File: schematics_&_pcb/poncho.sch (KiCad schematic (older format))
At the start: 4 parts, among them P1 CONN_20X2, P2 CONN_20X2, P3 ESP8266

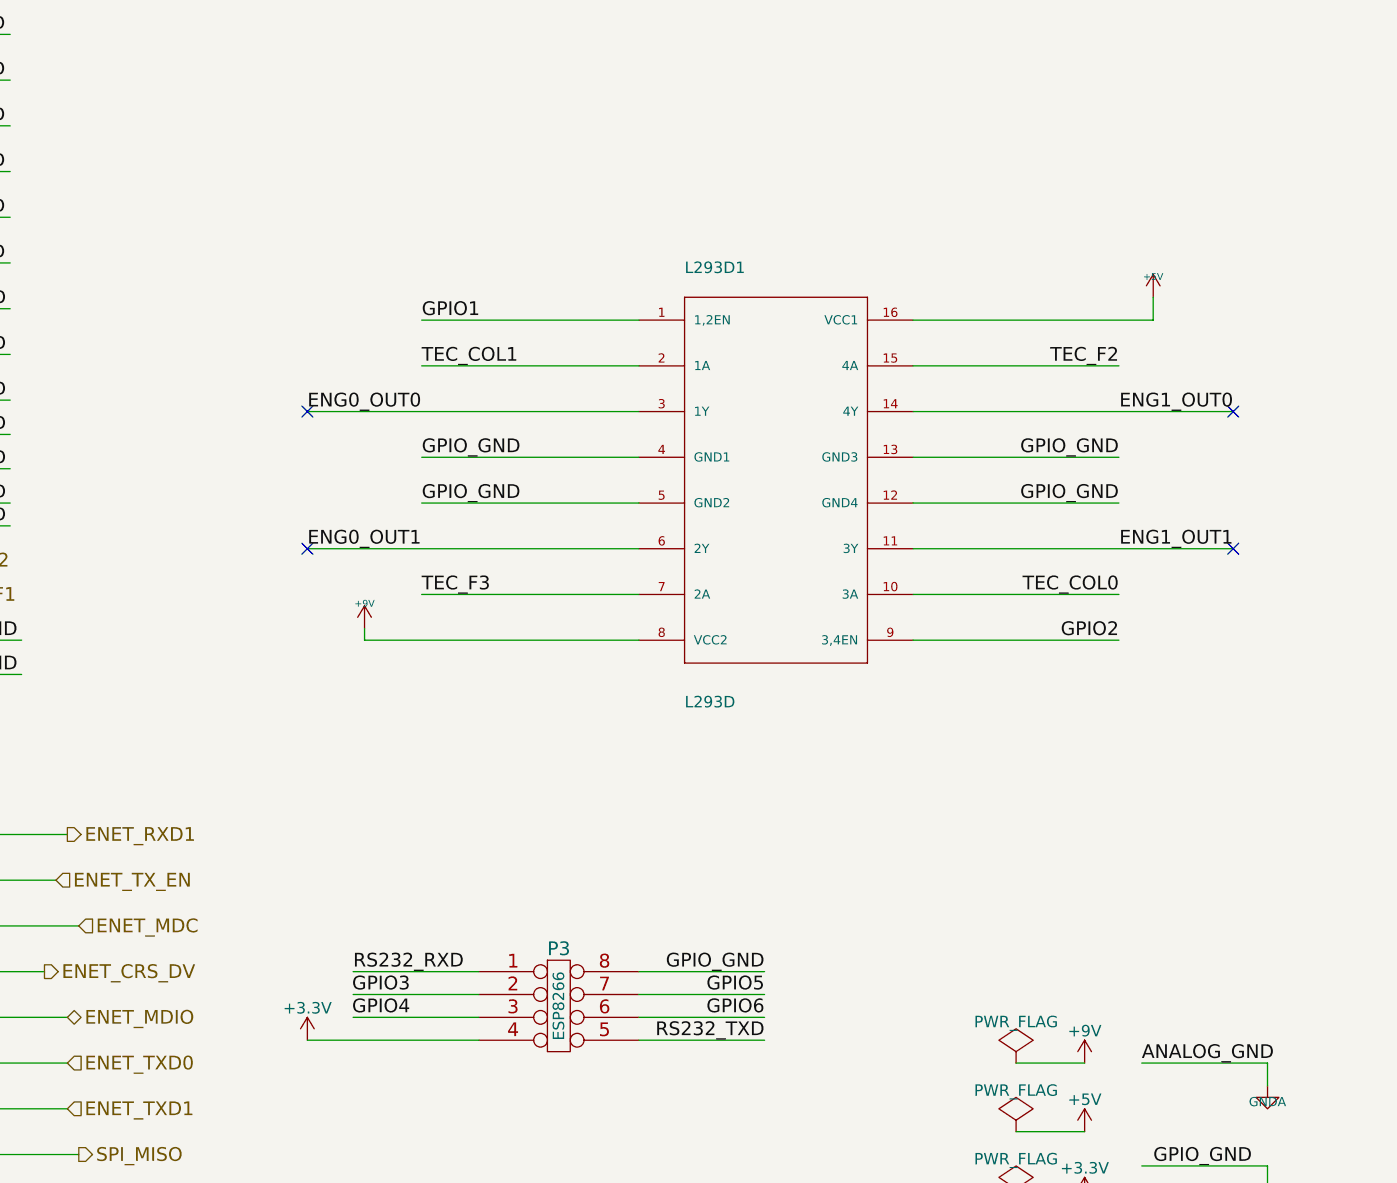
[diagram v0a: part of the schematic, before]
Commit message: Diagrama esquemático y PCB finalizados. [TODO] Verificar que sean correctos.
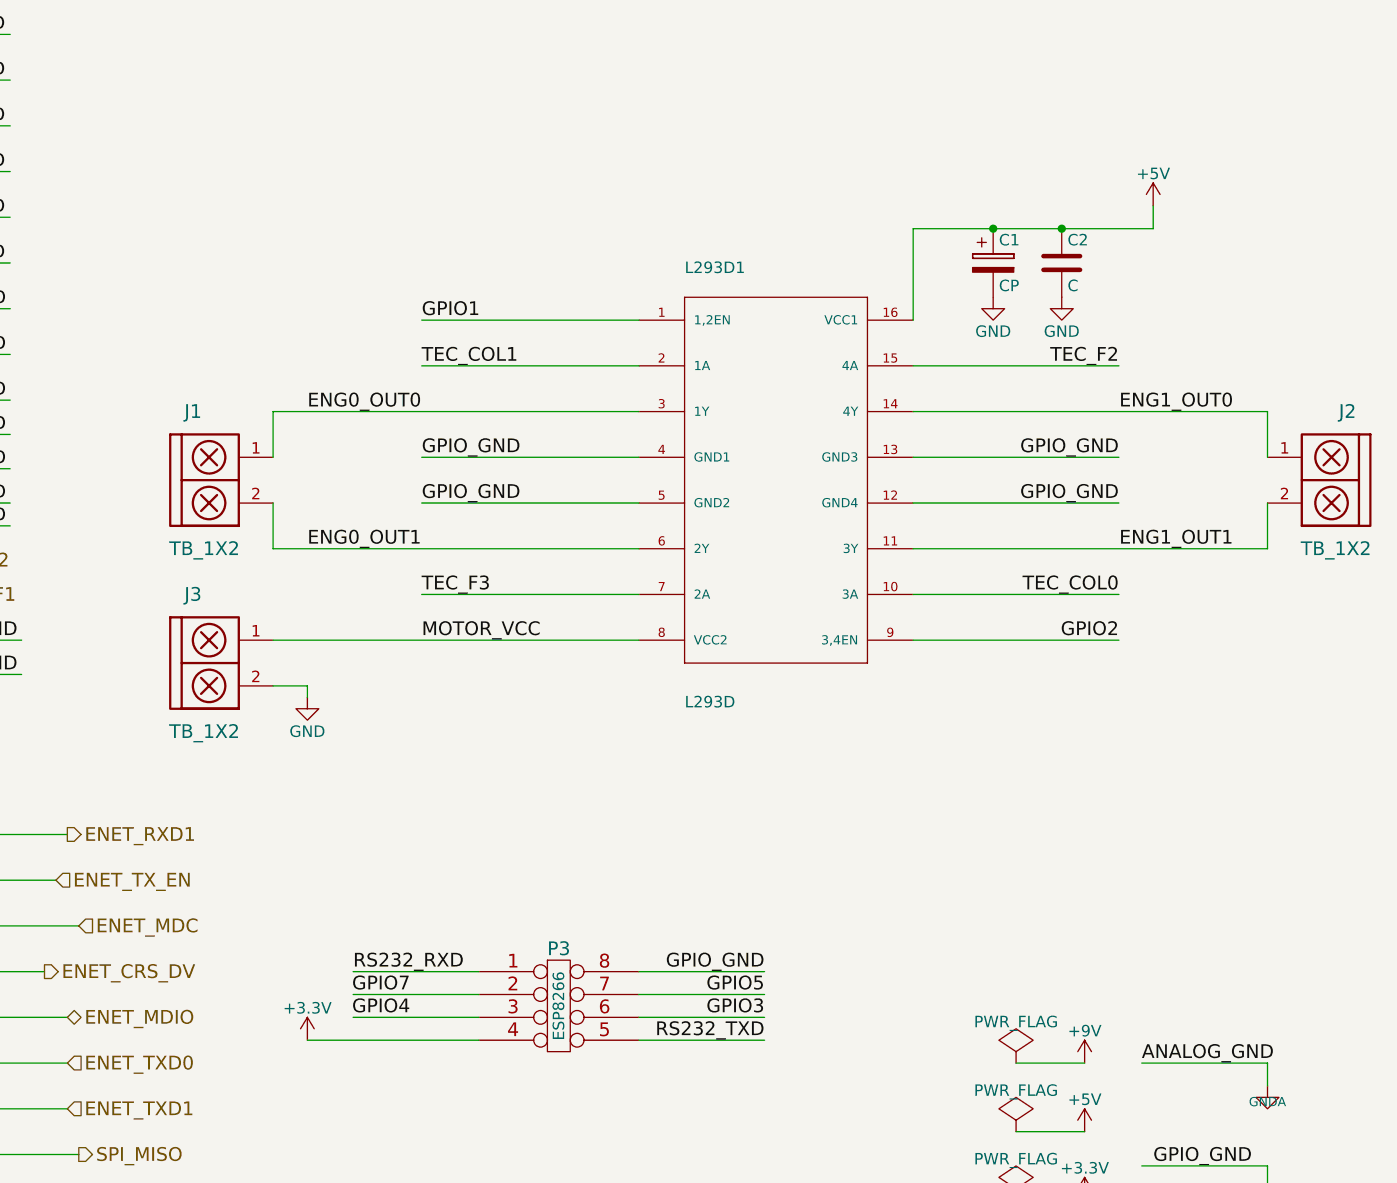
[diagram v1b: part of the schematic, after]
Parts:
- added C1: CP, Capacitors_Elko_ThroughHole:Elko_vert_11.2x6.3mm_RM2.5, symbol CP
- added C2: C, Capacitors_ThroughHole:C_Disc_D3_P2.5, symbol C
- added J1, J2, J3: TB_1X2, Pin_Headers:Pin_Header_Straight_1x02, symbol TB_1X2
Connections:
- net labels added: MOTOR_VCC
- wire segments 261 -> 267
- no-connect marks 4 -> 0
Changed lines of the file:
@@
 LIBS:valves
 LIBS:stepper drivers
+LIBS:edu-ciaa-nxp
+LIBS:terminal_block
 LIBS:poncho-cache
 EELAYER 25 0
@@
 F 3 "" H 8500 2900 60  0000 C CNN
 	1    8500 2900
-	1    0    0    -1
-$EndComp
-$Comp
-L +9V #PWR01
-U 1 1 560AA652
-P 6700 3550
-F 0 "#PWR01" H 6700 3520 20  0001 C CNN
-F 1 "+9V" H 6700 3660 30  0000 C CNN
-F 2 "" H 6700 3550 60  0000 C CNN
-F 3 "" H 6700 3550 60  0000 C CNN
-	1    6700 3550
-	1    0    0    -1
-$EndComp
-$Comp
-L +5V #PWR02
-U 1 1 560AA653
-P 10150 2100
-F 0 "#PWR02" H 10150 2190 20  0001 C CNN
-F 1 "+5V" H 10150 2190 30  0000 C CNN
-F 2 "" H 10150 2100 60  0000 C CNN
-F 3 "" H 10150 2100 60  0000 C CNN
-	1    10150 2100
 	1    0    0    -1
 $EndComp
@@
 ENG1_OUT1
 Wire Wire Line
-	6700 3600 6700 3550
-Wire Wire Line
-	6700 3600 7900 3600
+	6300 3600 7900 3600
 Wire Wire Line
 	6950 3000 7900 3000
@@
 	9100 3400 10000 3400
 Wire Wire Line
-	9100 2600 10500 2600
-Wire Wire Line
-	9100 3200 10500 3200
-Wire Wire Line
-	7900 3200 6450 3200
-Wire Wire Line
-	7900 2600 6450 2600
-Wire Wire Line
-	9100 2200 10150 2200
-Wire Wire Line
-	10150 2200 10150 2100
+	9100 2600 10650 2600
+Wire Wire Line
+	9100 3200 10650 3200
+Wire Wire Line
+	6300 3200 7900 3200
+Wire Wire Line
+	6300 2600 7900 2600
+Wire Wire Line
+	9100 1800 10150 1800
 Text HLabel 1100 6750 0    60   BiDi ~ 0
 GPIO0
@@
 WAKEUP
 $Comp
-L +3.3V #PWR03
+L +3.3V #PWR01
 U 1 1 52CA1E6C
 P 2450 750
-F 0 "#PWR03" H 2450 710 30  0001 C CNN
+F 0 "#PWR01" H 2450 710 30  0001 C CNN
 F 1 "+3.3V" H 2450 860 30  0000 C CNN
 F 2 "" H 2450 750 60  0000 C CNN
@@
 SPI_MOSI
 $Comp
-L GNDA #PWR04
+L GNDA #PWR02
 U 1 1 52DEB0D0
 P 10650 5550
-F 0 "#PWR04" H 10650 5550 40  0001 C CNN
+F 0 "#PWR02" H 10650 5550 40  0001 C CNN
 F 1 "GNDA" H 10650 5480 40  0000 C CNN
 F 2 "" H 10650 5550 60  0000 C CNN
@@
 $EndComp
 $Comp
-L +5V #PWR05
+L +5V #PWR03
 U 1 1 539535EE
 P 3450 750
-F 0 "#PWR05" H 3450 840 20  0001 C CNN
+F 0 "#PWR03" H 3450 840 20  0001 C CNN
 F 1 "+5V" H 3450 840 30  0000 C CNN
 F 2 "" H 3450 750 60  0000 C CNN
@@
 RESET
 $Comp
-L +3.3V #PWR06
+L +3.3V #PWR04
 U 1 1 539E165A
 P 2900 4550
-F 0 "#PWR06" H 2900 4510 30  0001 C CNN
+F 0 "#PWR04" H 2900 4510 30  0001 C CNN
 F 1 "+3.3V" H 2900 4660 30  0000 C CNN
 F 2 "" H 2900 4550 60  0000 C CNN
@@
 $EndComp
 $Comp
-L +5V #PWR07
+L +5V #PWR05
 U 1 1 539E1666
 P 3900 4550
-F 0 "#PWR07" H 3900 4640 20  0001 C CNN
+F 0 "#PWR05" H 3900 4640 20  0001 C CNN
 F 1 "+5V" H 3900 4640 30  0000 C CNN
 F 2 "" H 3900 4550 60  0000 C CNN
@@
 $EndComp
 $Comp
-L GND #PWR08
+L GND #PWR06
 U 1 1 53B8B104
 P 10650 6050
-F 0 "#PWR08" H 10650 6050 30  0001 C CNN
+F 0 "#PWR06" H 10650 6050 30  0001 C CNN
 F 1 "GND" H 10650 5980 30  0001 C CNN
 F 2 "" H 10650 6050 60  0000 C CNN
@@
 Text Label 10000 3400 2    60   ~ 0
 TEC_COL0
-NoConn ~ 6450 2600
-NoConn ~ 6450 3200
-NoConn ~ 10500 2600
-NoConn ~ 10500 3200
-$Comp
-L +9V #PWR09
+$Comp
+L +9V #PWR07
 U 1 1 561305A1
 P 9850 5450
-F 0 "#PWR09" H 9850 5300 50  0001 C CNN
+F 0 "#PWR07" H 9850 5300 50  0001 C CNN
 F 1 "+9V" H 9850 5590 50  0000 C CNN
 F 2 "" H 9850 5450 60  0000 C CNN
@@
 $EndComp
 $Comp
-L +3.3V #PWR010
+L +3.3V #PWR08
 U 1 1 561305C0
 P 9850 6050
-F 0 "#PWR010" H 9850 5900 50  0001 C CNN
+F 0 "#PWR08" H 9850 5900 50  0001 C CNN
 F 1 "+3.3V" H 9850 6190 50  0000 C CNN
 F 2 "" H 9850 6050 60  0000 C CNN
@@
 $EndComp
 $Comp
-L +5V #PWR011
+L +5V #PWR09
 U 1 1 56130604
 P 9850 5750
-F 0 "#PWR011" H 9850 5600 50  0001 C CNN
+F 0 "#PWR09" H 9850 5600 50  0001 C CNN
 F 1 "+5V" H 9850 5890 50  0000 C CNN
 F 2 "" H 9850 5750 60  0000 C CNN
@@
 $EndComp
 $Comp
-L PWR_FLAG #FLG012
+L PWR_FLAG #FLG010
 U 1 1 56130623
 P 9550 5750
-F 0 "#FLG012" H 9550 5845 50  0001 C CNN
+F 0 "#FLG010" H 9550 5845 50  0001 C CNN
 F 1 "PWR_FLAG" H 9550 5930 50  0000 C CNN
 F 2 "" H 9550 5750 60  0000 C CNN
@@
 $EndComp
 $Comp
-L PWR_FLAG #FLG013
+L PWR_FLAG #FLG011
 U 1 1 56130642
 P 9550 5450
-F 0 "#FLG013" H 9550 5545 50  0001 C CNN
+F 0 "#FLG011" H 9550 5545 50  0001 C CNN
 F 1 "PWR_FLAG" H 9550 5630 50  0000 C CNN
 F 2 "" H 9550 5450 60  0000 C CNN
@@
 $EndComp
 $Comp
-L PWR_FLAG #FLG014
+L PWR_FLAG #FLG012
 U 1 1 56130661
 P 9550 6050
-F 0 "#FLG014" H 9550 6145 50  0001 C CNN
+F 0 "#FLG012" H 9550 6145 50  0001 C CNN
 F 1 "PWR_FLAG" H 9550 6230 50  0000 C CNN
 F 2 "" H 9550 6050 60  0000 C CNN
@@
 GPIO_GND
 $Comp
-L +3.3V #PWR015
+L +3.3V #PWR013
 U 1 1 56131FC1
 P 6450 5350
-F 0 "#PWR015" H 6450 5200 50  0001 C CNN
+F 0 "#PWR013" H 6450 5200 50  0001 C CNN
 F 1 "+3.3V" H 6450 5490 50  0000 C CNN
 F 2 "" H 6450 5350 60  0000 C CNN
@@
 $EndComp
 Text Label 6900 5150 2    60   ~ 0
-GPIO3
+GPIO7
 Text Label 6900 5250 2    60   ~ 0
 GPIO4
@@
 GPIO5
 Text Label 8450 5250 2    60   ~ 0
-GPIO6
+GPIO3
+$Comp
+L C C2
+U 1 1 5616E701
+P 9750 1950
+F 0 "C2" H 9775 2050 50  0000 L CNN
+F 1 "C" H 9775 1850 50  0000 L CNN
+F 2 "Capacitors_ThroughHole:C_Disc_D3_P2.5" H 9788 1800 30  0001 C CNN
+F 3 "" H 9750 1950 60  0000 C CNN
+	1    9750 1950
+	1    0    0    -1
+$EndComp
+$Comp
+L CP C1
+U 1 1 5616E747
+P 9450 1950
+F 0 "C1" H 9475 2050 50  0000 L CNN
+F 1 "CP" H 9475 1850 50  0000 L CNN
+F 2 "Capacitors_Elko_ThroughHole:Elko_vert_11.2x6.3mm_RM2.5" H 9488 1800 30  0001 C CNN
+F 3 "" H 9450 1950 60  0000 C CNN
+	1    9450 1950
+	1    0    0    -1
+$EndComp
+$Comp
+L GND #PWR014
+U 1 1 5616E8DA
+P 9750 2100
+F 0 "#PWR014" H 9750 1850 50  0001 C CNN
+F 1 "GND" H 9750 1950 50  0000 C CNN
+F 2 "" H 9750 2100 60  0000 C CNN
+F 3 "" H 9750 2100 60  0000 C CNN
+	1    9750 2100
+	1    0    0    -1
+$EndComp
+$Comp
+L GND #PWR015
+U 1 1 5616E8F4
+P 9450 2100
+F 0 "#PWR015" H 9450 1850 50  0001 C CNN
+F 1 "GND" H 9450 1950 50  0000 C CNN
+F 2 "" H 9450 2100 60  0000 C CNN
+F 3 "" H 9450 2100 60  0000 C CNN
+	1    9450 2100
+	1    0    0    -1
+$EndComp
+Connection ~ 9750 1800
+Wire Wire Line
+	9100 1800 9100 2200
+Connection ~ 9450 1800
+$Comp
+L +5V #PWR016
+U 1 1 5616EDA1
+P 10150 1700
+F 0 "#PWR016" H 10150 1550 50  0001 C CNN
+F 1 "+5V" H 10150 1840 50  0000 C CNN
+F 2 "" H 10150 1700 60  0000 C CNN
+F 3 "" H 10150 1700 60  0000 C CNN
+	1    10150 1700
+	1    0    0    -1
+$EndComp
+Wire Wire Line
+	10150 1800 10150 1700
+$Comp
+L TB_1X2 J1
+U 1 1 56175CA0
+P 5950 2900
+F 0 "J1" H 5950 3200 60  0000 C CNN
+F 1 "TB_1X2" H 6000 2600 60  0000 C CNN
+F 2 "Pin_Headers:Pin_Header_Straight_1x02" H 5900 2950 60  0001 C CNN
+F 3 "" H 5900 2950 60  0000 C CNN
+	1    5950 2900
+	1    0    0    -1
+$EndComp
+Wire Wire Line
+	6300 2600 6300 2800
+Wire Wire Line
+	6300 3000 6300 3200
+$Comp
+L TB_1X2 J2
+U 1 1 56175F83
+P 11000 2900
+F 0 "J2" H 11000 3200 60  0000 C CNN
+F 1 "TB_1X2" H 11050 2600 60  0000 C CNN
+F 2 "Pin_Headers:Pin_Header_Straight_1x02" H 10950 2950 60  0001 C CNN
+F 3 "" H 10950 2950 60  0000 C CNN
+	1    11000 2900
+	-1   0    0    -1
+$EndComp
+Wire Wire Line
+	10650 2600 10650 2800
+Wire Wire Line
+	10650 3200 10650 3000
+$Comp
+L TB_1X2 J3
+U 1 1 56176549
+P 5950 3700
+F 0 "J3" H 5950 4000 60  0000 C CNN
+F 1 "TB_1X2" H 6000 3400 60  0000 C CNN
+F 2 "Pin_Headers:Pin_Header_Straight_1x02" H 5900 3750 60  0001 C CNN
+F 3 "" H 5900 3750 60  0000 C CNN
+	1    5950 3700
+	1    0    0    -1
+$EndComp
+$Comp
+L GND #PWR017
+U 1 1 561766BA
+P 6450 3850
+F 0 "#PWR017" H 6450 3600 50  0001 C CNN
+F 1 "GND" H 6450 3700 50  0000 C CNN
+F 2 "" H 6450 3850 60  0000 C CNN
+F 3 "" H 6450 3850 60  0000 C CNN
+	1    6450 3850
+	1    0    0    -1
+$EndComp
+Wire Wire Line
+	6450 3850 6450 3800
+Wire Wire Line
+	6450 3800 6300 3800
+Text Label 6950 3600 0    60   ~ 0
+MOTOR_VCC
 $EndSCHEMATC

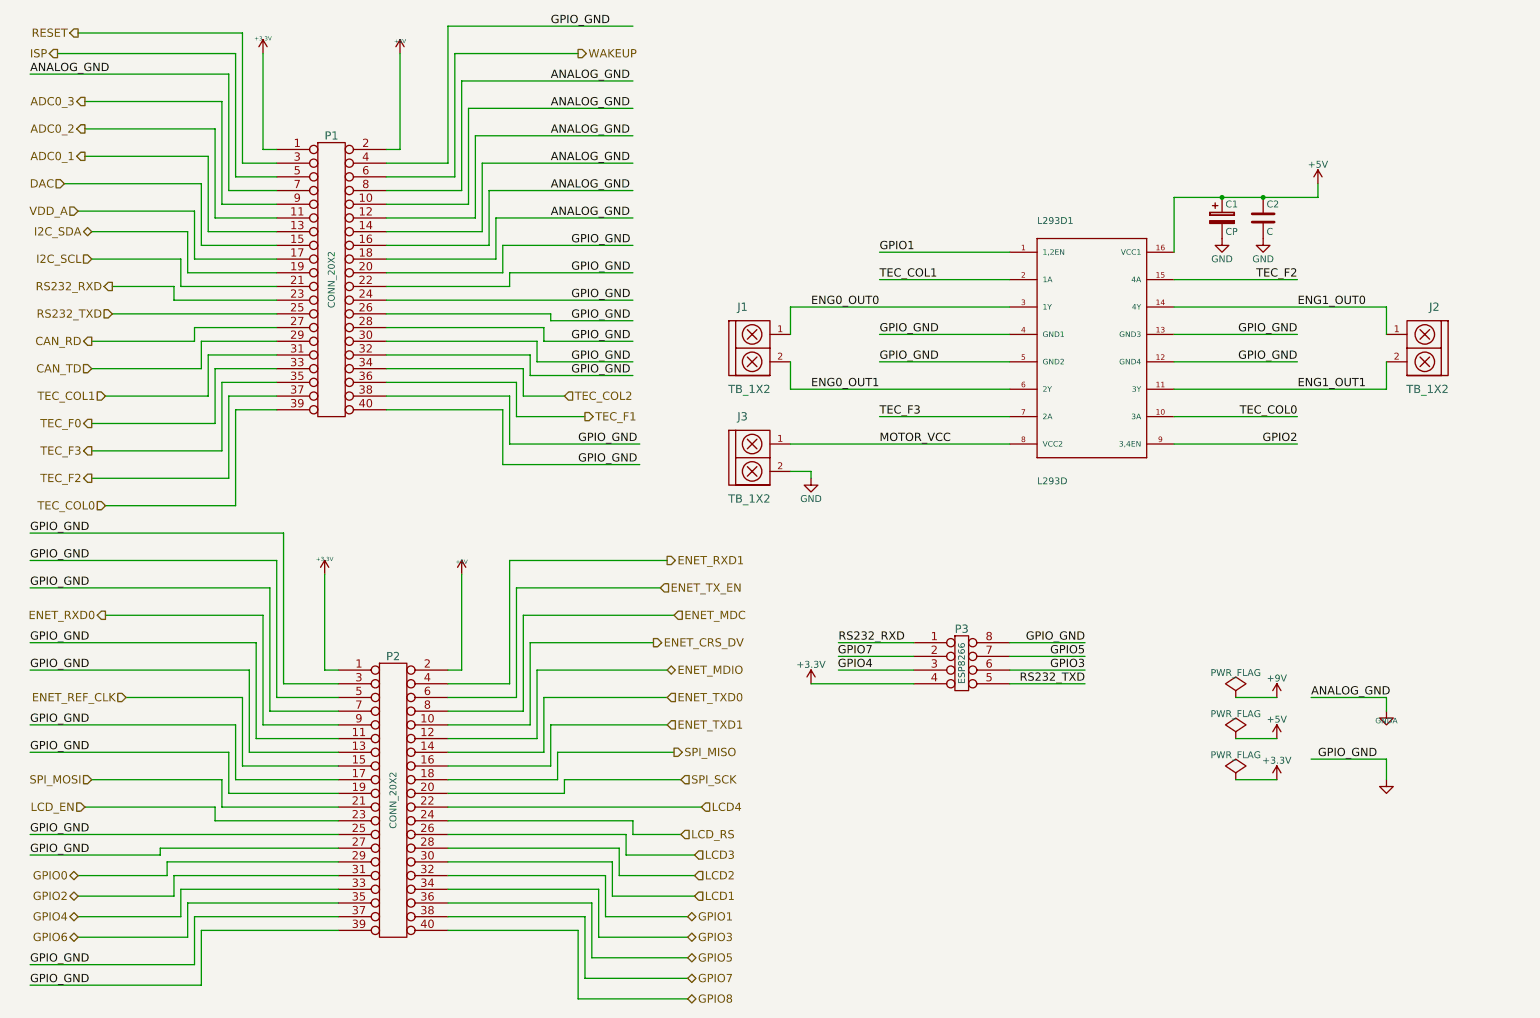
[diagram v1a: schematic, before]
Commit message: PCB modificado. [TODO] Verificar que esté correcto y proceder a armar la placa.
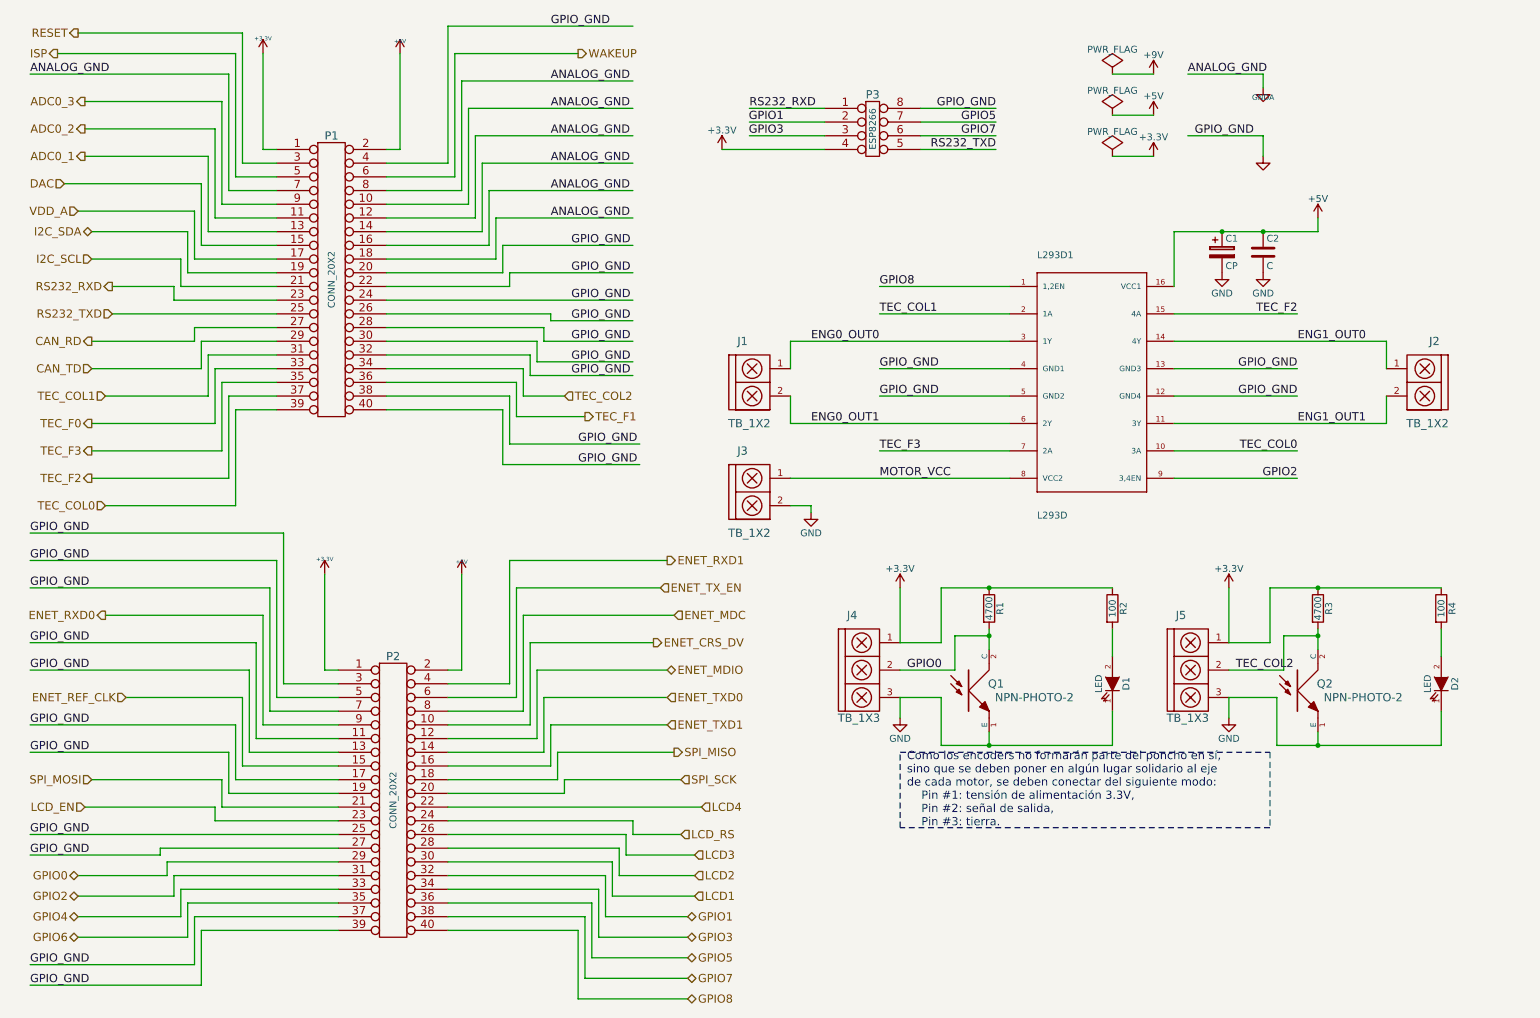
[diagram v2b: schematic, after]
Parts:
- added D1, D2: LED, LEDs:LED-5MM, symbol LED
- added J4, J5: TB_1X3, Pin_Headers:Pin_Header_Straight_1x03, symbol TB_1X3
- added Q1, Q2: NPN-PHOTO-2, modules:PHOTOTRANS-5MM, symbol NPN-PHOTO-2
- added R1, R3: 4700, Resistors_ThroughHole:Resistor_Horizontal_RM10mm, symbol R
- added R2, R4: 100, Resistors_ThroughHole:Resistor_Horizontal_RM10mm, symbol R
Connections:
- wire segments 267 -> 297
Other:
- note added: "Como los encoders no formarán parte del poncho en sí, \nsino que se deben poner en algún lugar solidario al eje \nde cada motor, se deben conectar del siguiente modo:\n Pin #1: tensión de alimentación 3.3V,\n Pin #2: señal de salida,\n Pin #3: tierra."
- moved on the sheet: C1, C2, J1, J2, J3, L293D1, P3

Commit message: .pcb y .sch modificados.
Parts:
- added J6, J7: TB_1X3, Pin_Headers:Pin_Header_Straight_1x03, symbol TB_1X3
- D1, D2: symbol LED -> LED-RESCUE-poncho
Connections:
- wire segments 297 -> 307
- no-connect marks 0 -> 2
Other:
- moved on the sheet: P3
